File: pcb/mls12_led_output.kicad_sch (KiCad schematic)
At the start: 18 parts, among them J4 JST B3B-ZR, J5 DC barrel plug, Q1 DMG3406L, Q2 DMG3406L

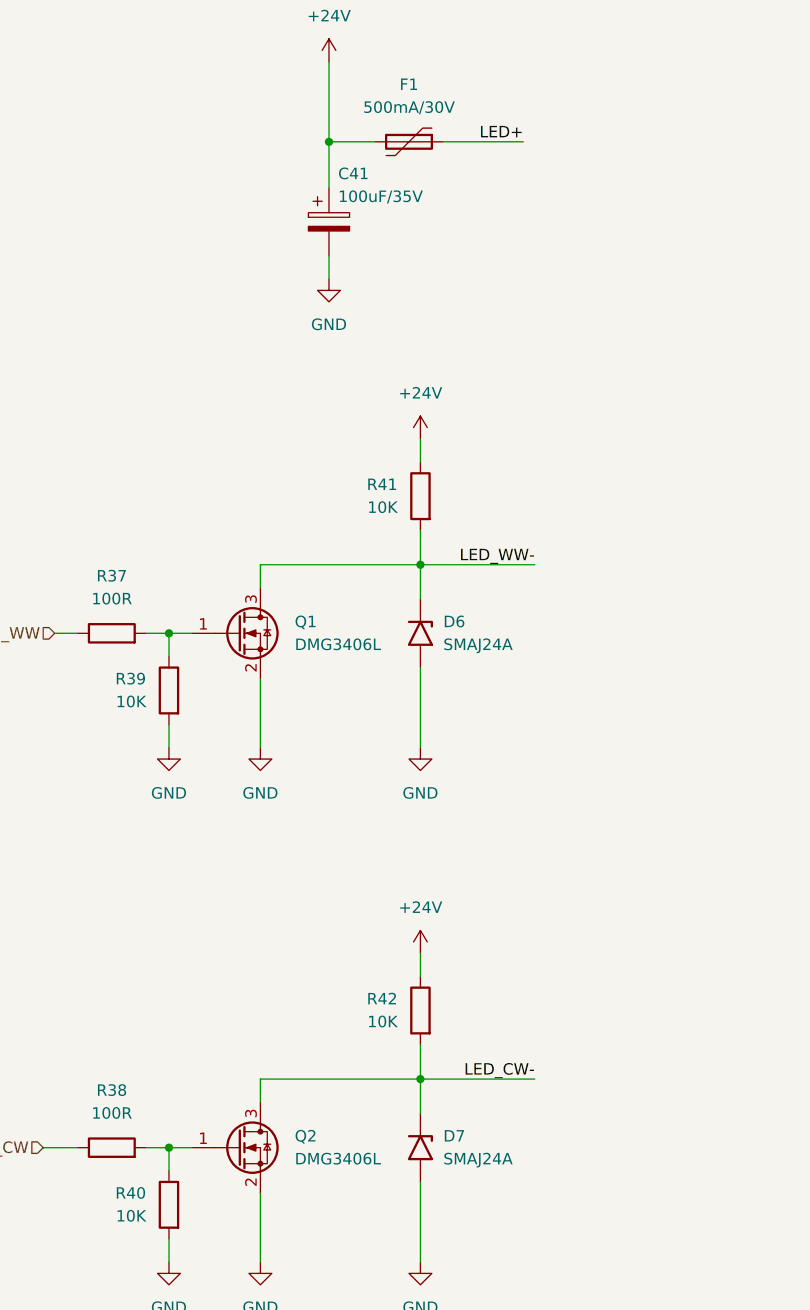
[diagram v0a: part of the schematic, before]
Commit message: Update to 25W PoE+ module, 2 outputs
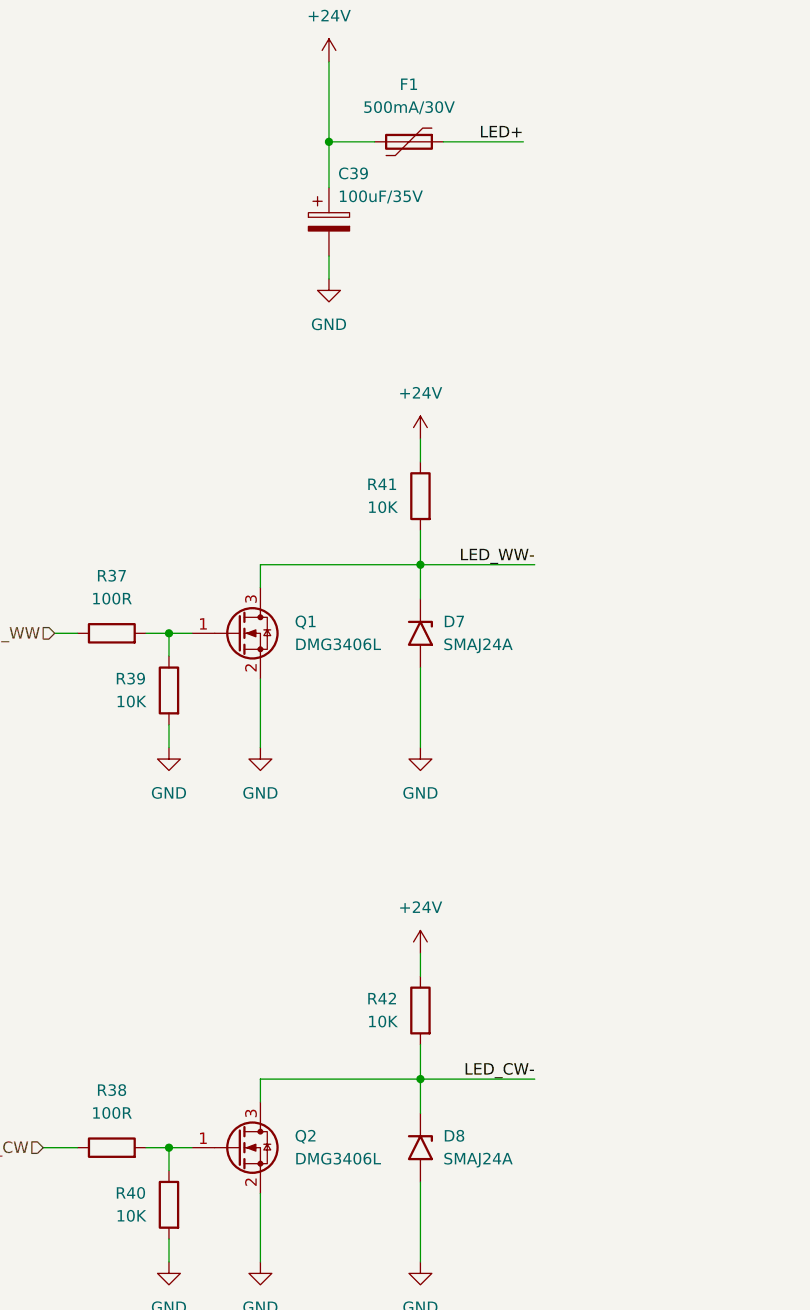
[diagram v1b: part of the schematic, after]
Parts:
- renumbered C41 to C39, D6 to D7, D7 to D8
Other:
- company: (none) -> Quomodo BV

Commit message: Add polyfuse footprint
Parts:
- F1: footprint (none) -> mls12:SMD1812B050TF_30
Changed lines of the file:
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@@
 			)
 		)
-		(property "Footprint" ""
+		(property "Footprint" "mls12:SMD1812B050TF_30"
 			(at 86.36 46.99 0)
 			(effects

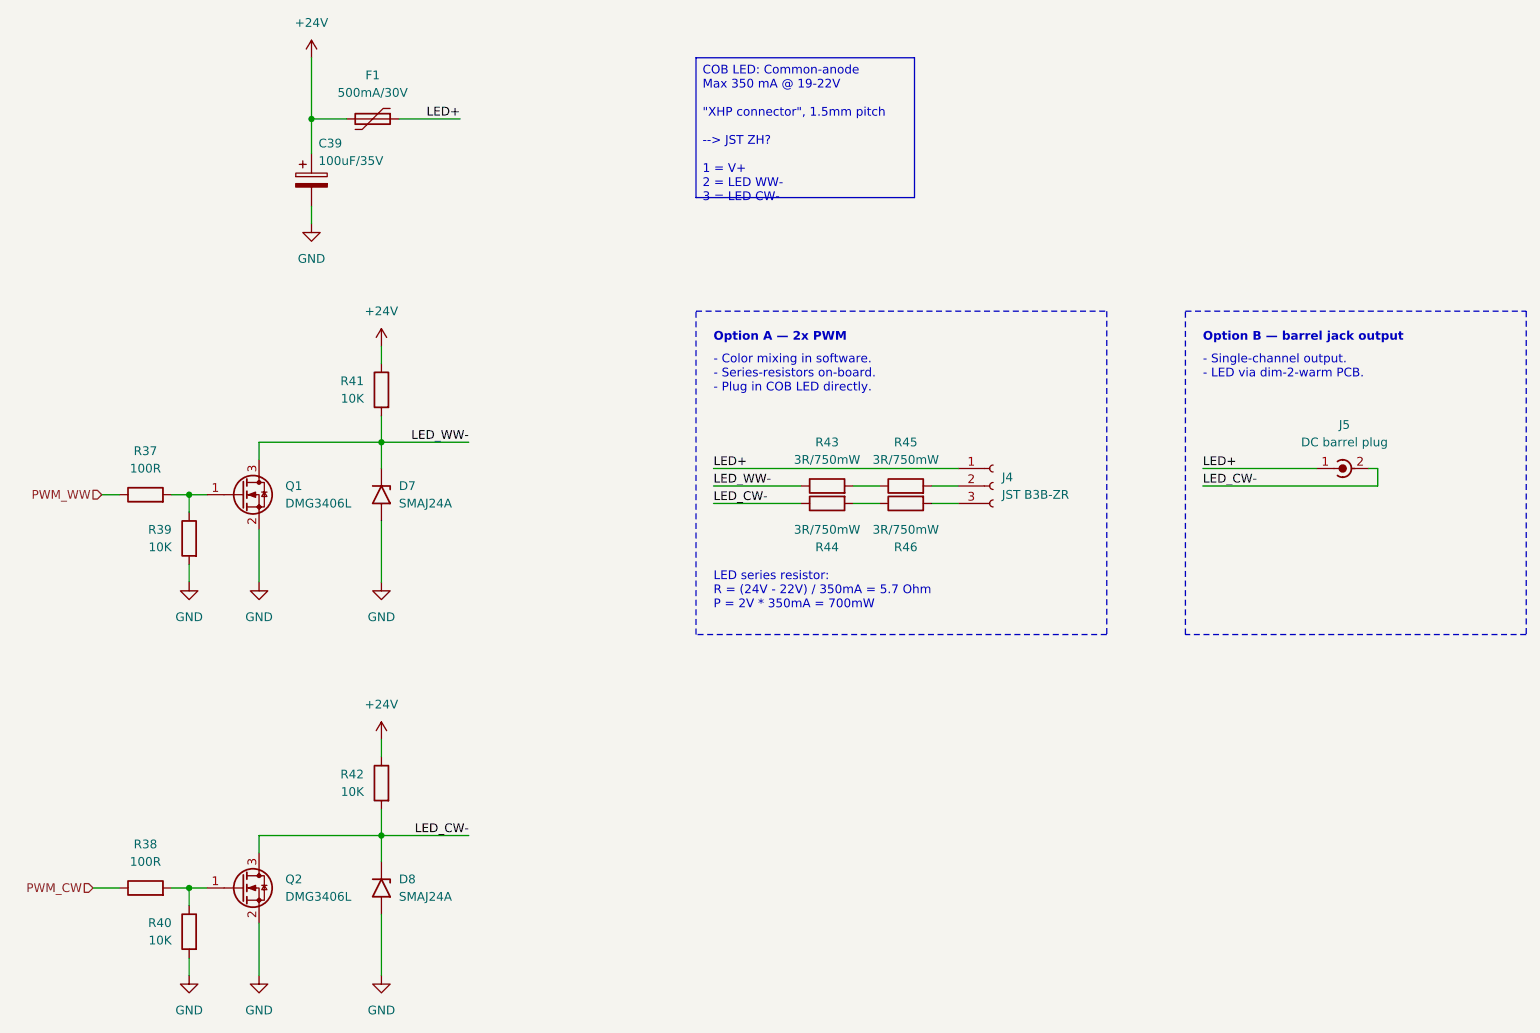
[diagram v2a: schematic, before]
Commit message: Add test points
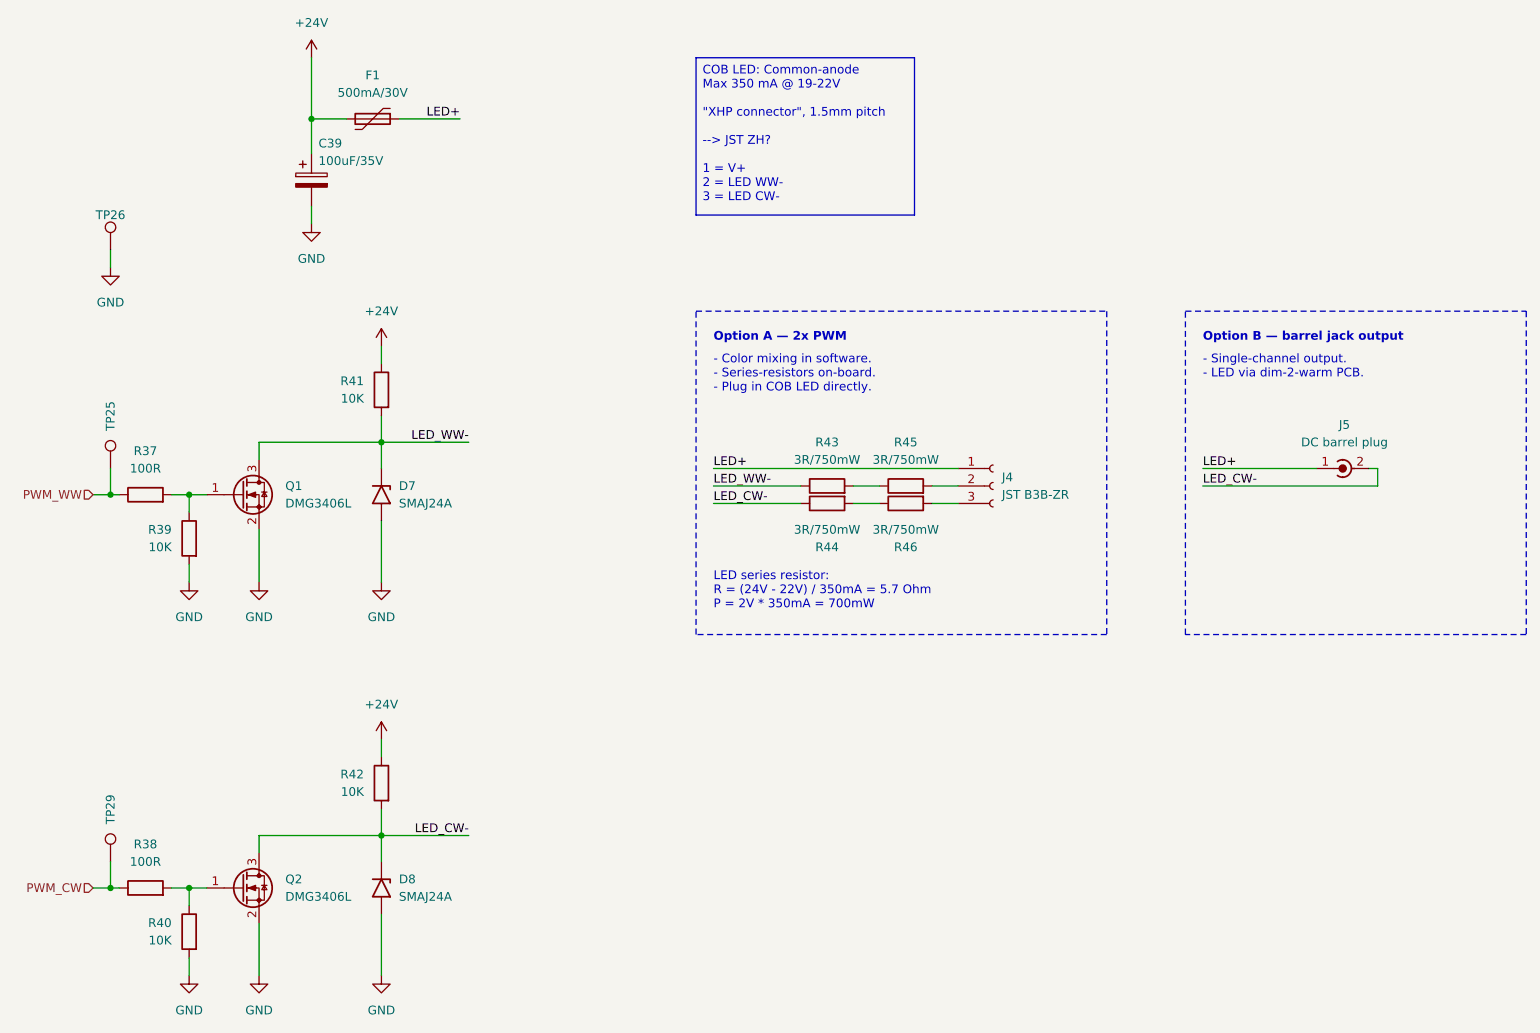
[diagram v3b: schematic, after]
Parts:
- added TP25, TP29: TestPoint, TestPoint:TestPoint_Pad_D1.5mm, symbol Connector:TestPoint
- added TP26: TestPoint, TestPoint:TestPoint_Pad_1.5x1.5mm, symbol Connector:TestPoint
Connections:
- net GND: now also TP26.1
- net PWM_CW: now also TP29.1
- net PWM_WW: now also TP25.1
